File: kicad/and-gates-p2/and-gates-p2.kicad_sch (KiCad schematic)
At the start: 28 parts

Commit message: Update and export schematics
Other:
- note added: "The pull-up input tied with the gate forms a voltage divisor going through R6/D5/R2 (and R6/D4/R5). That will make outputs quite high even when both inputs are low. The input with pull-down solves that issue (it also reverses the behaviour of the push-button, making them "high" on released and "low" when pressed). However the chained gates show another problem. When B is low, and the rest of the 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"
- company: (none) -> Silicon Chronicles
- title: Diodes & Diodes (Building AND gates the wrong way: Part 2) -> Diodes & Diodes
- moved on the sheet: D1, D10, D11, D12, D4, D5, D6, D7, D8, D9, R1, R11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

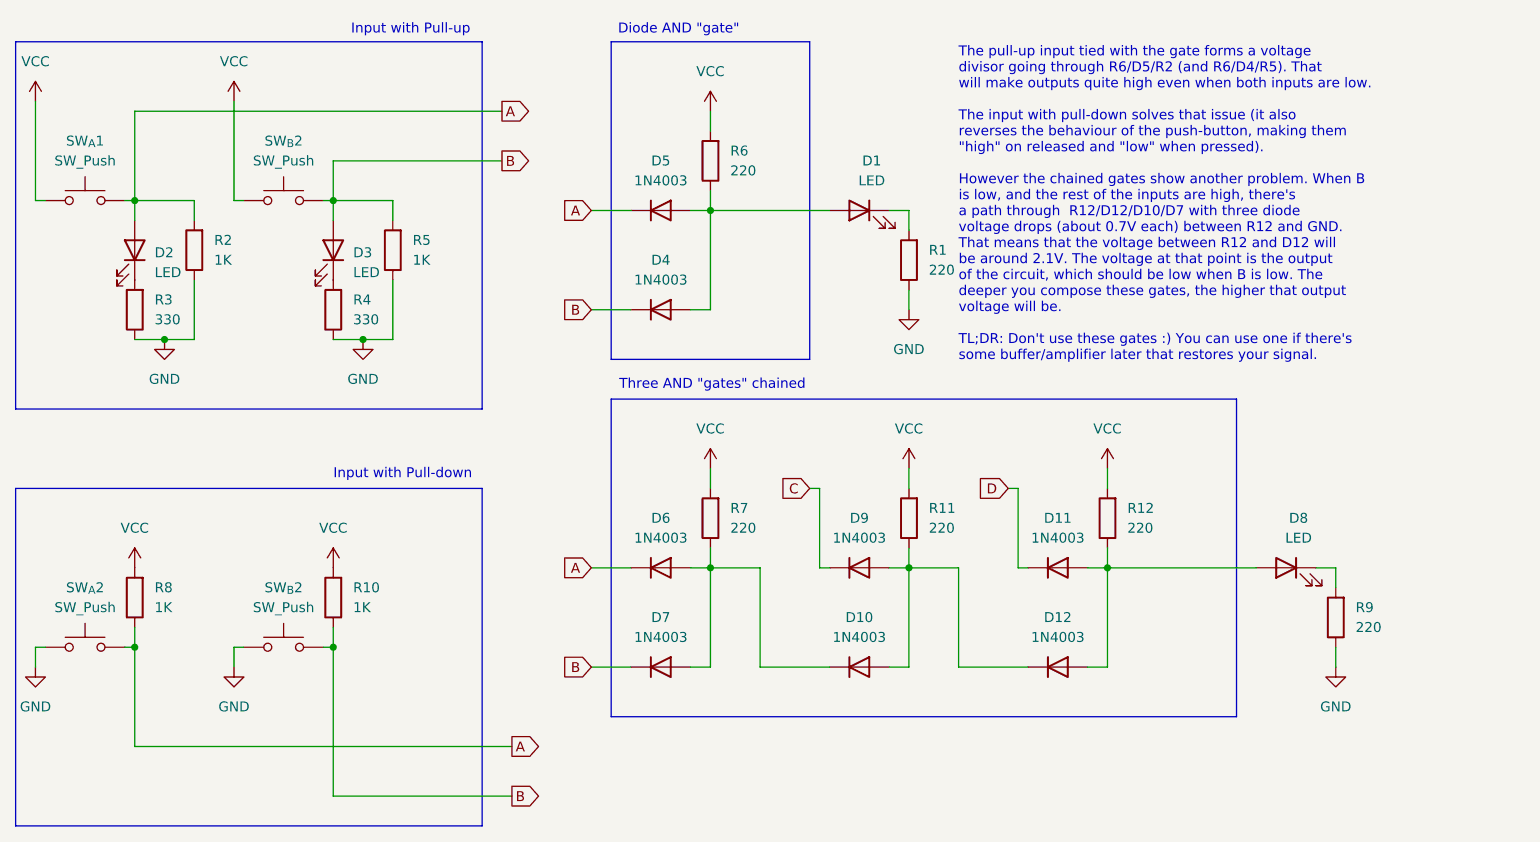
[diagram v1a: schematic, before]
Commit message: Fix text in schematics (mixup between pull-up vs pull-down)
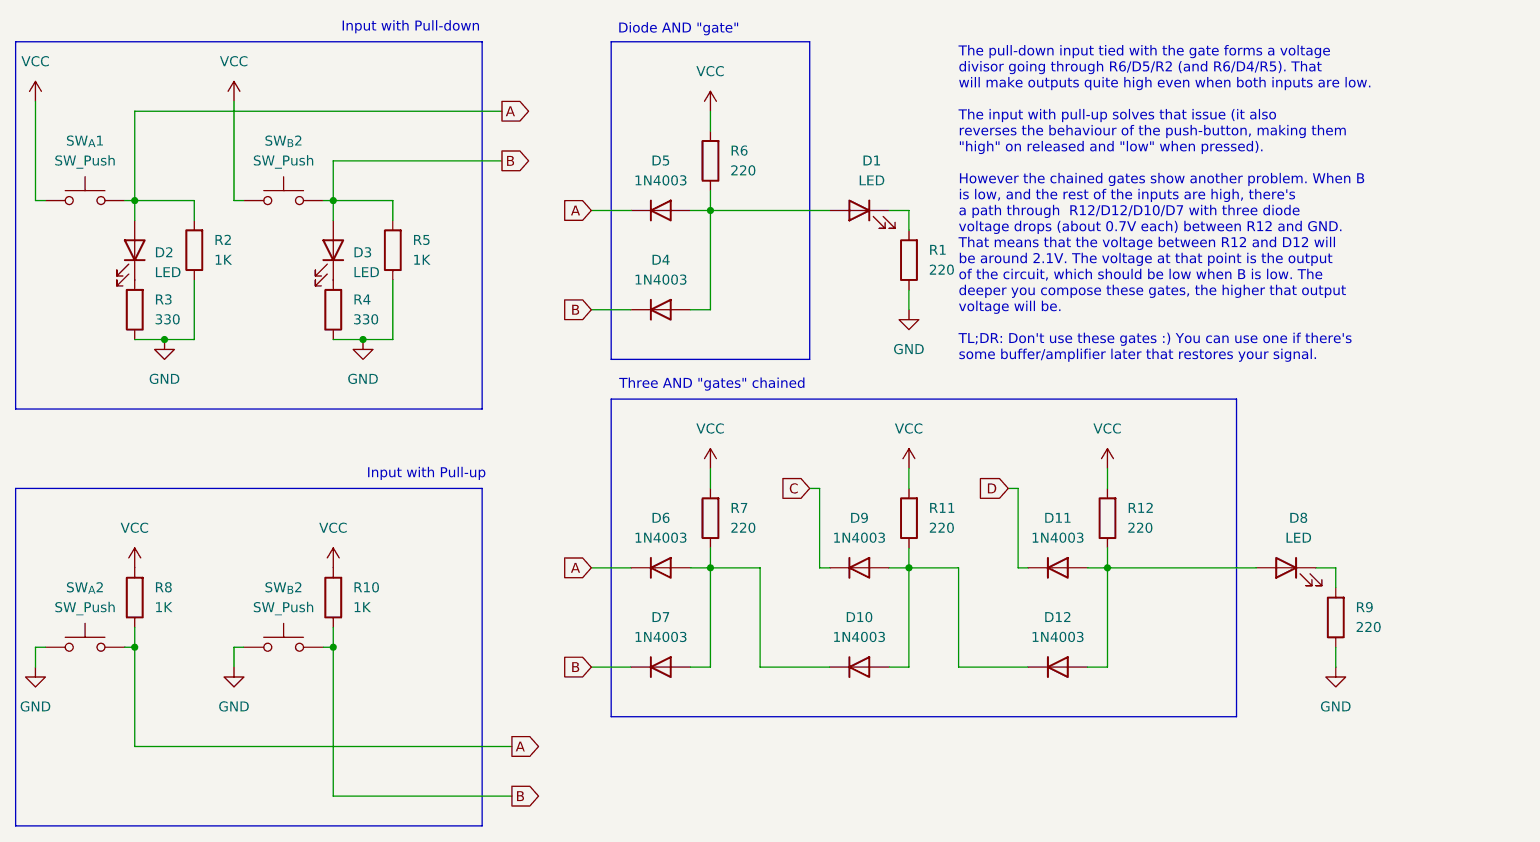
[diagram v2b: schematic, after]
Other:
- note added: "The pull-down input tied with the gate forms a voltage divisor going through R6/D5/R2 (and R6/D4/R5). That will make outputs quite high even when both inputs are low. The input with pull-up solves that issue (it also reverses the behaviour of the push-button, making them "high" on released and "low" when pressed). However the chained gates show another problem. When B is low, and the rest of the 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"
- note removed: "The pull-up input tied with the gate forms a voltage divisor going through R6/D5/R2 (and R6/D4/R5). That will make outputs quite high even when both inputs are low. The input with pull-down solves that issue (it also reverses the behaviour of the push-button, making them "high" on released and "low" when pressed). However the chained gates show another problem. When B is low, and the rest of the 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"
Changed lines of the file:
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@@
 		)
 	)
-	(text "Input with Pull-up"
+	(text "Input with Pull-down"
 		(exclude_from_sim no)
-		(at 67.056 14.986 0)
+		(at 75.946 14.732 0)
 		(effects
 			(font
 				(size 1.27 1.27)
 			)
+			(justify right)
 		)
 	)
-	(text "The pull-up input tied with the gate forms a voltage\ndivisor going through R6/D5/R2 (and R6/D4/R5). That\nwill make outputs quite high even when both inputs are low.\n\nThe input with pull-down solves that issue (it also\nreverses the behaviour of the push-button, making them\n\"high\" on released and \"low\" when pressed).\n\nHowever the chained gates show another problem. When B\nis low, and the rest of the inputs are high, there's\na path through  R12/D12/D10/D7 with three diode\nvoltage drops (about 0.7V each) between R12 and GND.\nThat means that the voltage between R12 and D12 will\nbe around 2.1V. The voltage at that point is the output\nof the circuit, which should be low when B is low. The\ndeeper you compose these gates, the higher that output\nvoltage will be.\n\nTL;DR: Don't use these gates :) You can use one if there's\nsome buffer/amplifier later that restores your signal."
+	(text "The pull-down input tied with the gate forms a voltage\ndivisor going through R6/D5/R2 (and R6/D4/R5). That\nwill make outputs quite high even when both inputs are low.\n\nThe input with pull-up solves that issue (it also\nreverses the behaviour of the push-button, making them\n\"high\" on released and \"low\" when pressed).\n\nHowever the chained gates show another problem. When B\nis low, and the rest of the inputs are high, there's\na path through  R12/D12/D10/D7 with three diode\nvoltage drops (about 0.7V each) between R12 and GND.\nThat means that the voltage between R12 and D12 will\nbe around 2.1V. The voltage at that point is the output\nof the circuit, which should be low when B is low. The\ndeeper you compose these gates, the higher that output\nvoltage will be.\n\nTL;DR: Don't use these gates :) You can use one if there's\nsome buffer/amplifier later that restores your signal."
 		(exclude_from_sim no)
 		(at 137.16 37.338 0)
@@
 		)
 	)
-	(text "Input with Pull-down\n"
+	(text "Input with Pull-up\n"
 		(exclude_from_sim no)
-		(at 66.04 71.882 0)
+		(at 76.708 71.882 0)
 		(effects
 			(font
 				(size 1.27 1.27)
 			)
+			(justify right)
 		)
 	)
